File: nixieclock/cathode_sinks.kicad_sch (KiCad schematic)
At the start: 40 parts, among them Q10 BSS131, Q11 BSS131, Q12 BSS131, Q13 BSS131, Q14 BSS131, Q15 BSS131, Q16 BSS131, Q17 BSS131, Q18 BSS131, Q19 BSS131, Q20 BSS131, Q21 BSS131, Q22 BSS131, Q23 BSS131, Q24 BSS131, Q25 BSS131, Q26 BSS131, Q27 BSS131, Q28 BSS131, Q29 BSS131, Q3 BSS131, Q30 BSS131, Q31 BSS131, Q32 BSS131, Q33 BSS131, Q34 BSS131, Q35 BSS131, Q36 BSS131, Q37 BSS131, Q38 BSS131, Q39 BSS131, Q4 BSS131, Q40 BSS131, Q41 BSS131, Q42 BSS131, Q5 BSS131, Q6 BSS131, Q7 BSS131, Q8 BSS131, Q9 BSS131

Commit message: mostly finalized pcb layout, silkscreen graphics, etc
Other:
- company: (none) -> Bastian de Byl
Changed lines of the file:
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@@
   (title_block
     (title "Nixie Clock - Cathode Sinks")
-    (date "2021-03-18")
+    (date "2021-03-19")
+    (company "Bastian de Byl")
   )
   (bus_entry (at 46.99 20.32) (size 2.54 -2.54)

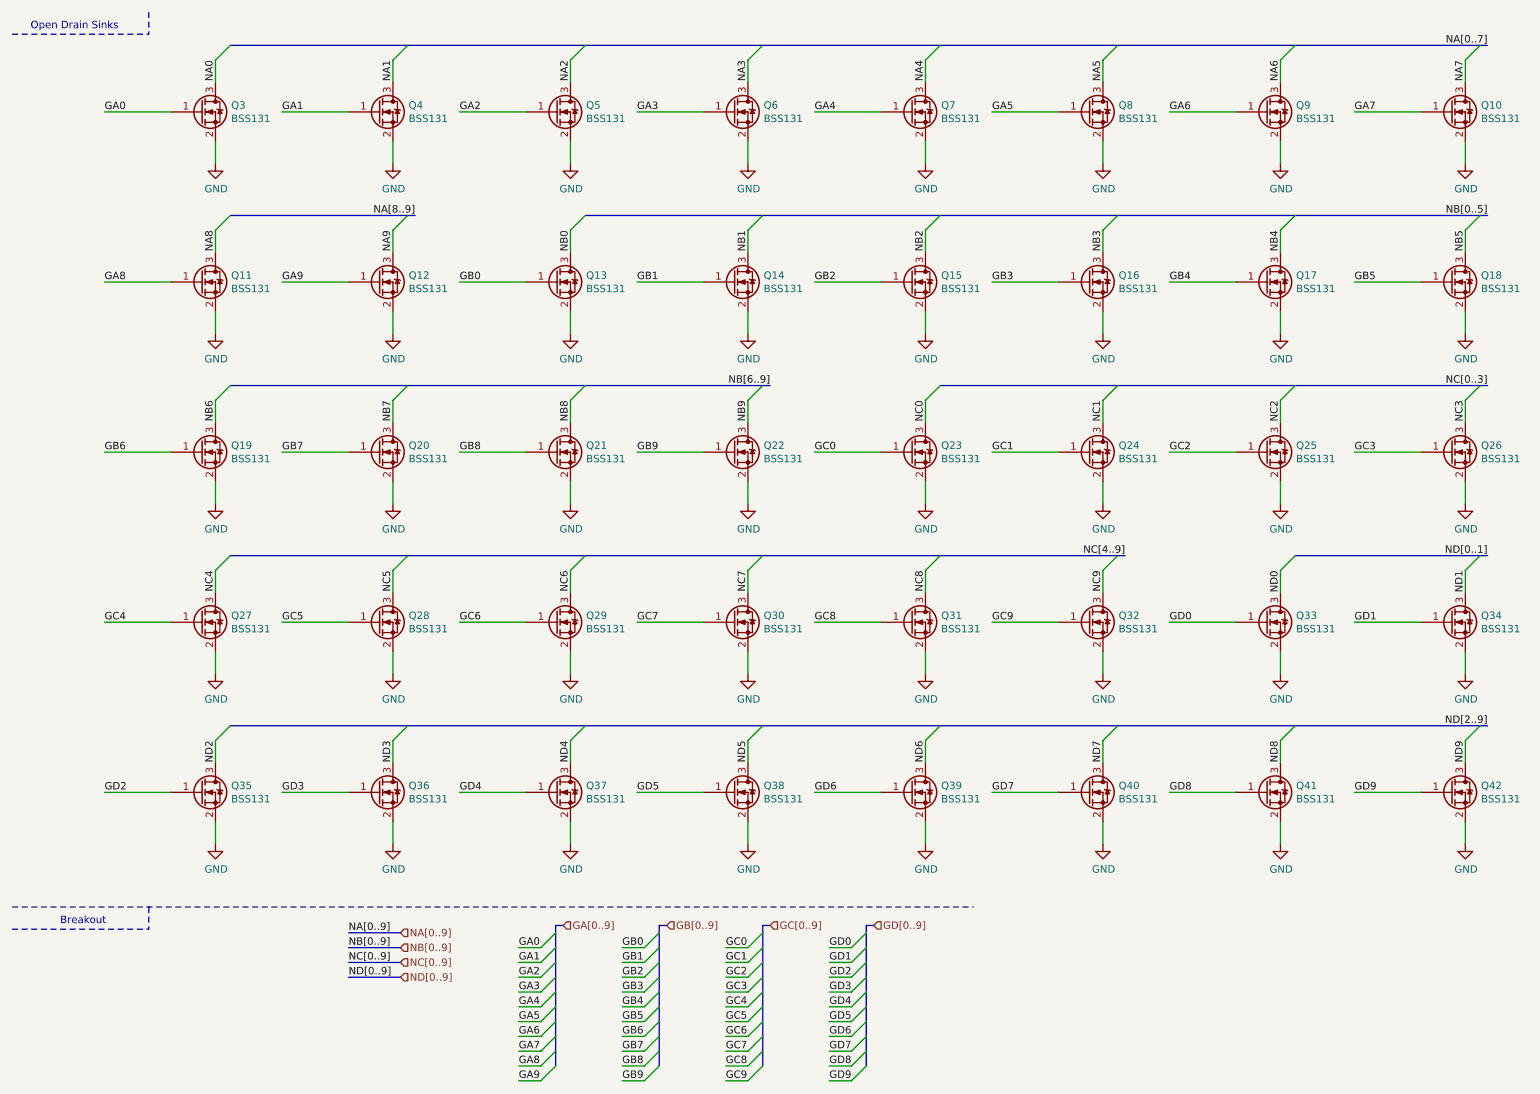
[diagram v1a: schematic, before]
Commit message: finalized neon bulb design (todo: pcb jumpers)
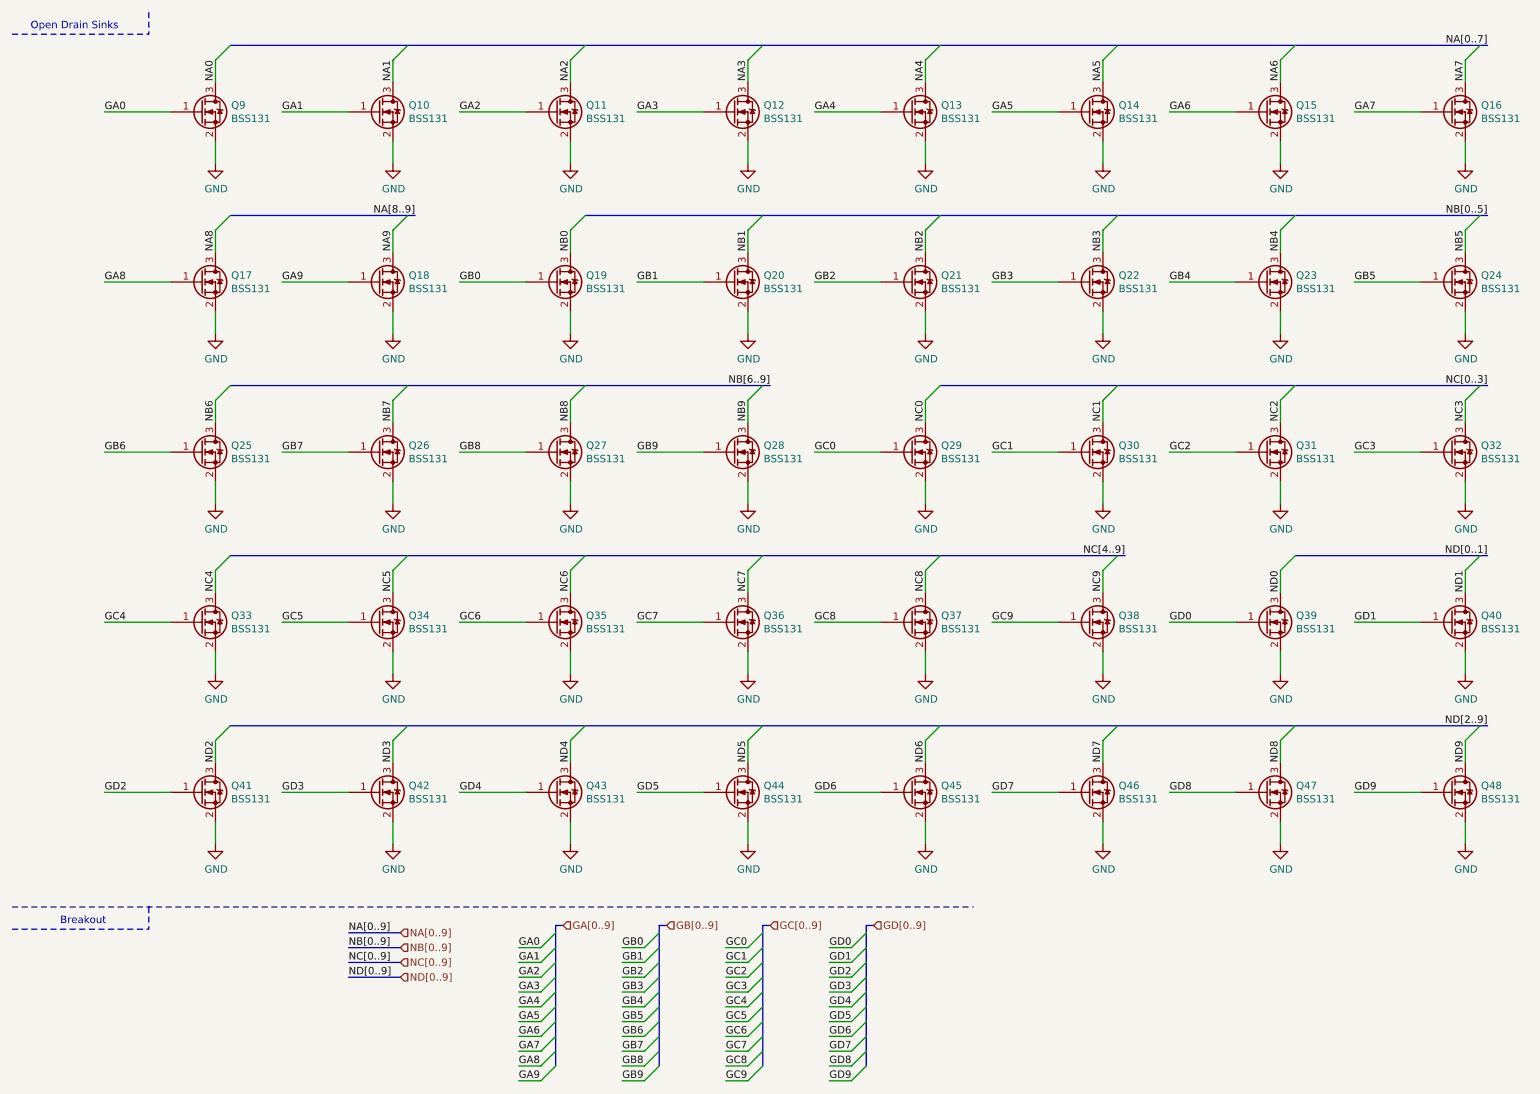
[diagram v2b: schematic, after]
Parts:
- renumbered Q4 to Q10, Q5 to Q11, Q6 to Q12, Q7 to Q13, Q8 to Q14, Q9 to Q15, Q10 to Q16, Q11 to Q17, Q12 to Q18, Q13 to Q19, Q14 to Q20, Q15 to Q21, Q16 to Q22, Q17 to Q23, Q18 to Q24, Q19 to Q25, Q20 to Q26, Q21 to Q27, Q22 to Q28, Q23 to Q29, Q24 to Q30, Q25 to Q31, Q26 to Q32, Q27 to Q33, Q28 to Q34, Q29 to Q35, Q30 to Q36, Q31 to Q37, Q32 to Q38, Q33 to Q39, Q34 to Q40, Q35 to Q41, Q36 to Q42, Q37 to Q43, Q38 to Q44, Q39 to Q45, Q40 to Q46, Q41 to Q47, Q42 to Q48, Q3 to Q9

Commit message: finalized design ready for quality check
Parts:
- added R35, R36, R37, R38, R39, R40, R41, R42, R43, R44, R45, R46, R47, R48, R49, R50, R51, R52, R53, R54, R55, R56, R57, R58, R59, R60, R61, R62, R63, R64, R65, R66, R67, R68, R69, R70, R71, R72, R73, R74: 1M, Resistor_SMD:R_0603_1608Metric_Pad1.05x0.95mm_HandSolder, symbol Device:R_Small
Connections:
- net GA0: now also R35.1
- net GA1: now also R36.1
- net GA2: now also R37.1
- net GA3: now also R38.1
- net GA4: now also R39.1
- net GA5: now also R40.1
- net GA6: now also R41.1
- net GA7: now also R42.1
- net GA8: now also R43.1
- net GA9: now also R44.1
- net GB0: now also R45.1
- net GB1: now also R46.1
- net GB2: now also R47.1
- net GB3: now also R48.1
- net GB4: now also R49.1
- net GB5: now also R50.1
- net GB6: now also R51.1
- net GB7: now also R52.1
- net GB8: now also R53.1
- net GB9: now also R54.1
- net GC0: now also R55.1
- net GC1: now also R56.1
- net GC2: now also R57.1
- net GC3: now also R58.1
- net GC4: now also R59.1
- net GC5: now also R60.1
- net GC6: now also R61.1
- net GC7: now also R62.1
- net GC8: now also R63.1
- net GC9: now also R64.1
- net GD0: now also R65.1
- net GD1: now also R66.1
- net GD2: now also R67.1
- net GD3: now also R68.1
- net GD4: now also R69.1
- net GD5: now also R70.1
- net GD6: now also R71.1
- net GD7: now also R72.1
- net GD8: now also R73.1
- net GD9: now also R74.1
- net GND: now also R35.2, R36.2, R37.2, R38.2, R39.2, R40.2, R41.2, R42.2, R43.2, R44.2, R45.2, R46.2, R47.2, R48.2, R49.2, R50.2, R51.2, R52.2, R53.2, R54.2, R55.2, R56.2, R57.2, R58.2, R59.2, R60.2, R61.2, R62.2, R63.2, R64.2, R65.2, R66.2, R67.2, R68.2, R69.2, R70.2, R71.2, R72.2, R73.2, R74.2
